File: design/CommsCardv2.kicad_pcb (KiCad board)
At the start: 4 copper layers, 191 parts, among them J1001 USB_B, J201 Conn_01x02, J301 DB9_Male_MountingHoles, J302 DB9_Male_MountingHoles, J303 DB9_Male_MountingHoles, J304 Conn_01x02, J305 Conn_Coaxial, J501 Conn_01x03, J701 Conn_01x03, J901 USB_B, Q301 Q_NMOS_DGS, Q302 Q_NMOS_DGS, U1001 ADUM3160, U201 LT3509EMSE, U301 MAX3387EEUG, U302 MAX3485, U303 TPS28225DRBT, U401 74LV14, U402 74LVC2G00, U403 STWD100xxWY, U404 STWD100xxWY, U405 74AHC157, U501 93C46B, U502 FT4232H, U503 74LV595, U601 74LVC3G14, U602 SN74LV86, U603 501BMILF, U604 74LVC1G80, U605 74LV595, U606 74LV595, U701 93C46B, U702 FT4232H, U703 74LV595, U801 74LVC3G14, U802 SN74LV86, U803 501BMILF, U804 74LVC1G80, U805 74LV595, U806 74LV595, U901 ADUM3160, X501 ASEMB-12MHz, X701 ASEMB-12MHz

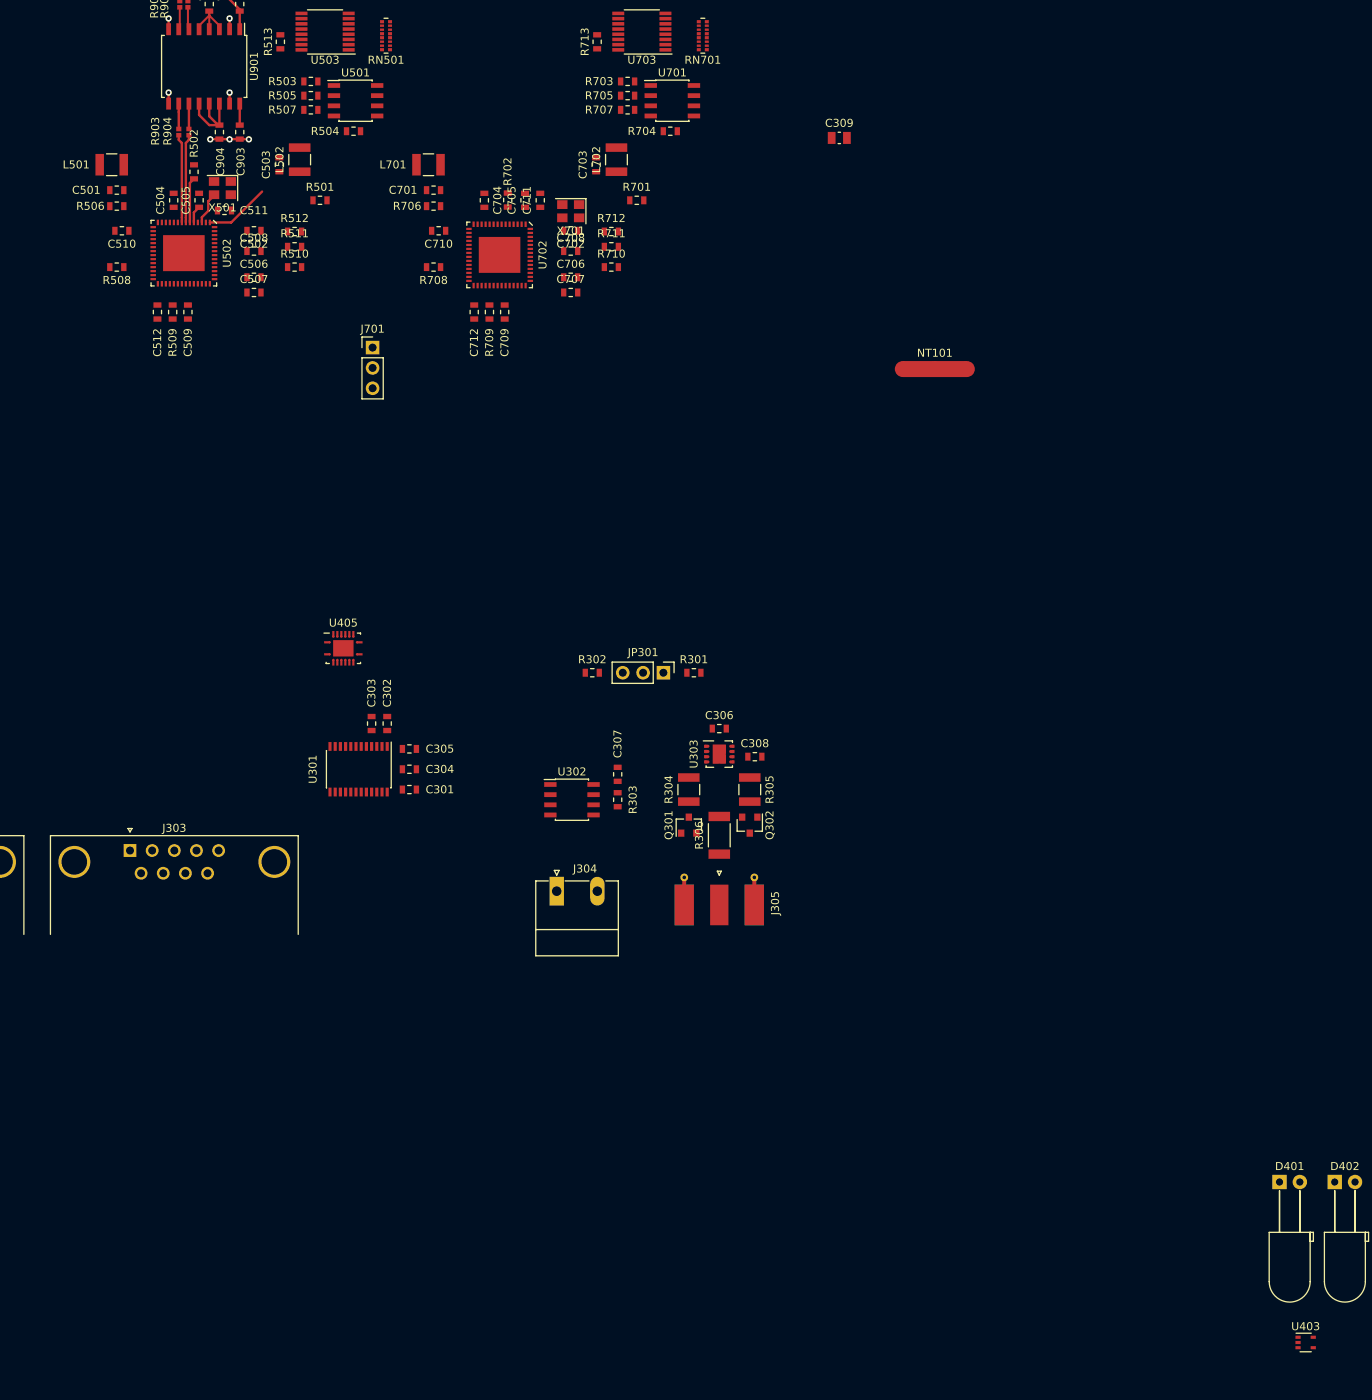
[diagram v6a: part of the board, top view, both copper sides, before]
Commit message: Layout FC1 FT Chip
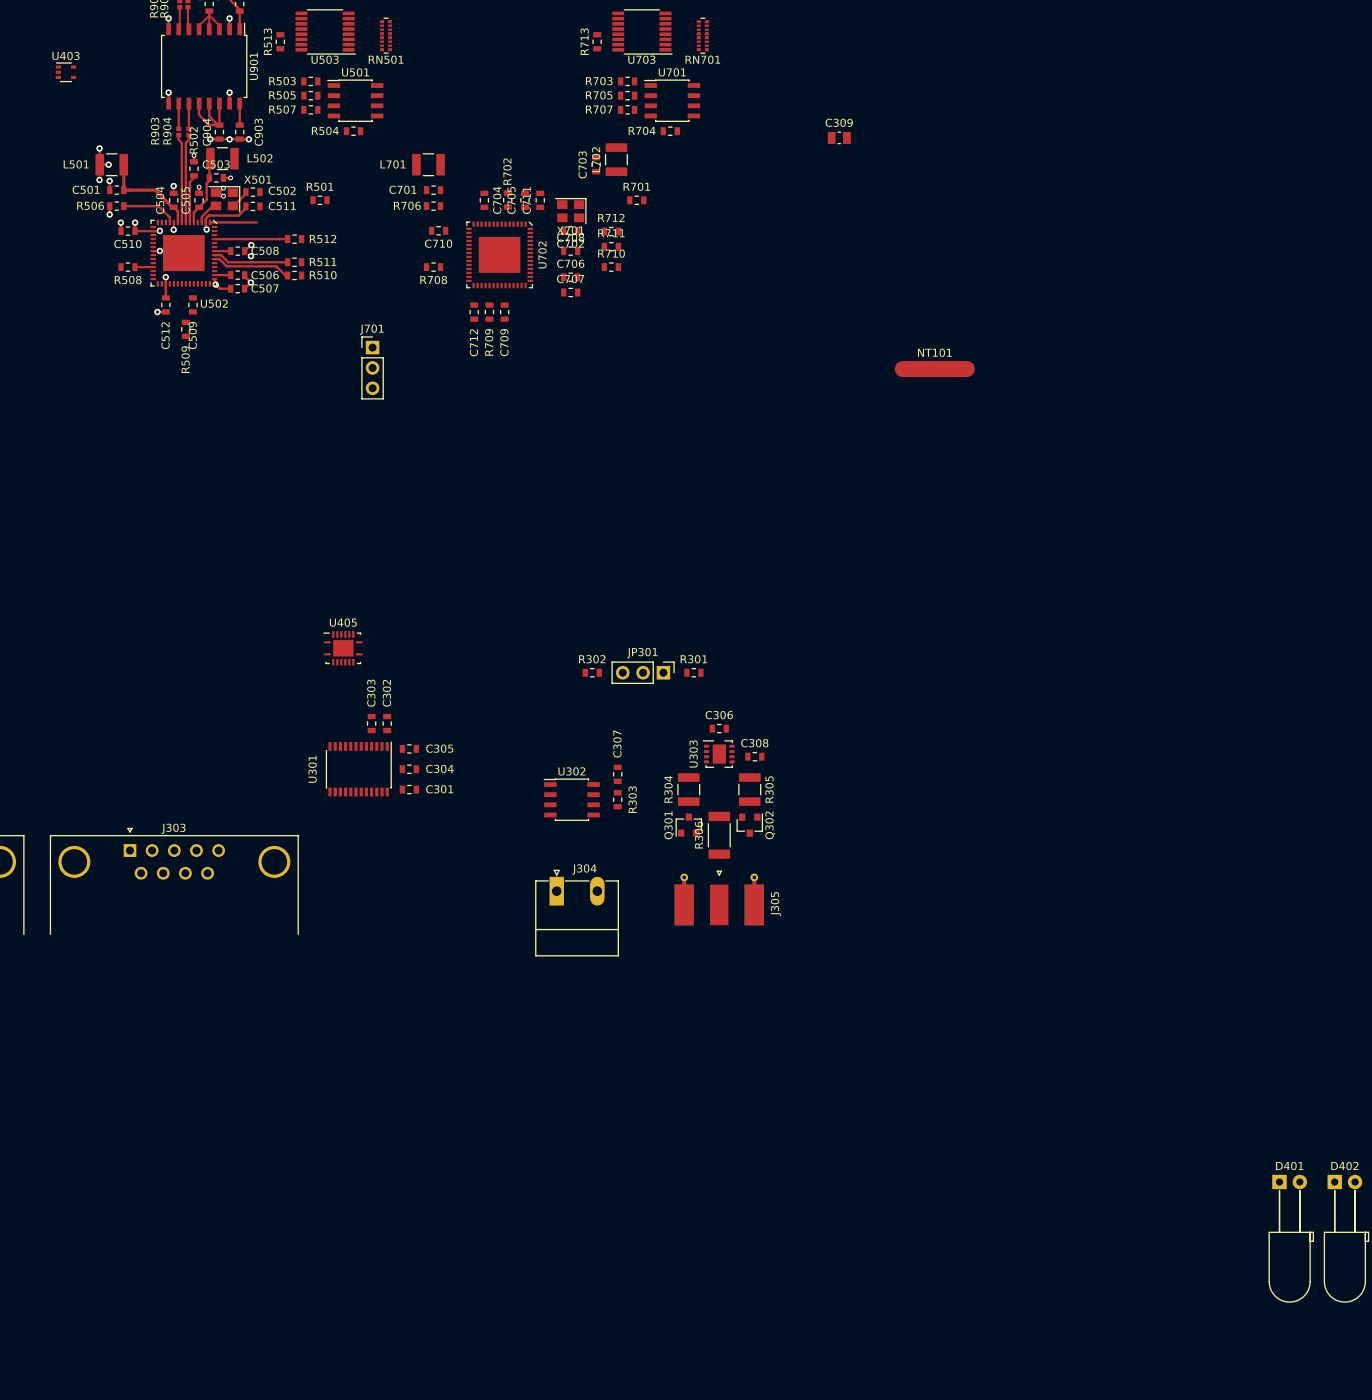
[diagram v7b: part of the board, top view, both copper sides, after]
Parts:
- moved U403 221.9 mm to (150.1, 55.1)
- moved L502 9.65 mm to (169.7, 65.9), turned to 0 degrees
- moved C503 8.05 mm to (168.9, 68.3), turned to 0 degrees
- moved C502 4.83 mm to (173.5, 70.1), turned to 0 degrees
- moved C511 3.59 mm to (173.5, 71.9)
- moved R509 2.72 mm to (165.1, 87.2)
- moved C507 2.09 mm to (171.6, 82.2)
- moved C506 2.05 mm to (171.6, 80.5)
- moved C508 2.03 mm to (171.6, 77.5)
- moved R511 1.94 mm to (178.7, 78.9)
- moved X501 1.42 mm to (169.9, 71.0)
- moved R508 1.40 mm to (157.9, 79.5)
- moved C512 1.38 mm to (162.6, 84.2)
- moved C509 1.09 mm to (166.0, 84.2)
- moved R510 1.05 mm to (178.7, 80.5)
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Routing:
- net +3V3: track 7.26 -> 24.1 mm, vias 2 -> 8
- net GND: track 30.1 -> 44.4 mm, vias 16 -> 30
- net /FlightComputer1/1V8: track 0.00 -> 12.7 mm, vias 0 -> 3
- net Net-(C501-Pad1): track 0.00 -> 12.4 mm
- net Net-(R510-Pad1): track 0.00 -> 9.98 mm
- net Net-(R511-Pad1): track 0.00 -> 9.50 mm
- net Net-(R512-Pad1): track 0.00 -> 9.13 mm
- net Net-(R506-Pad2): track 0.00 -> 6.96 mm
- net Net-(C503-Pad1): track 2.17 -> 8.84 mm
- net Net-(R508-Pad1): track 0.00 -> 2.28 mm
- net /FlightComputer1/EECS: track 8.13 -> 5.87 mm
- net /FlightComputer1/OSCI: track 4.10 -> 3.05 mm
- added copper zone on PWR2.Cu, net +3V3
- added copper zone on PWR2.Cu, net /FlightComputer1/1V8
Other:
- net class GND added: clearance 0.2, trace_width 0.3, via_dia 0.6, via_drill 0.35

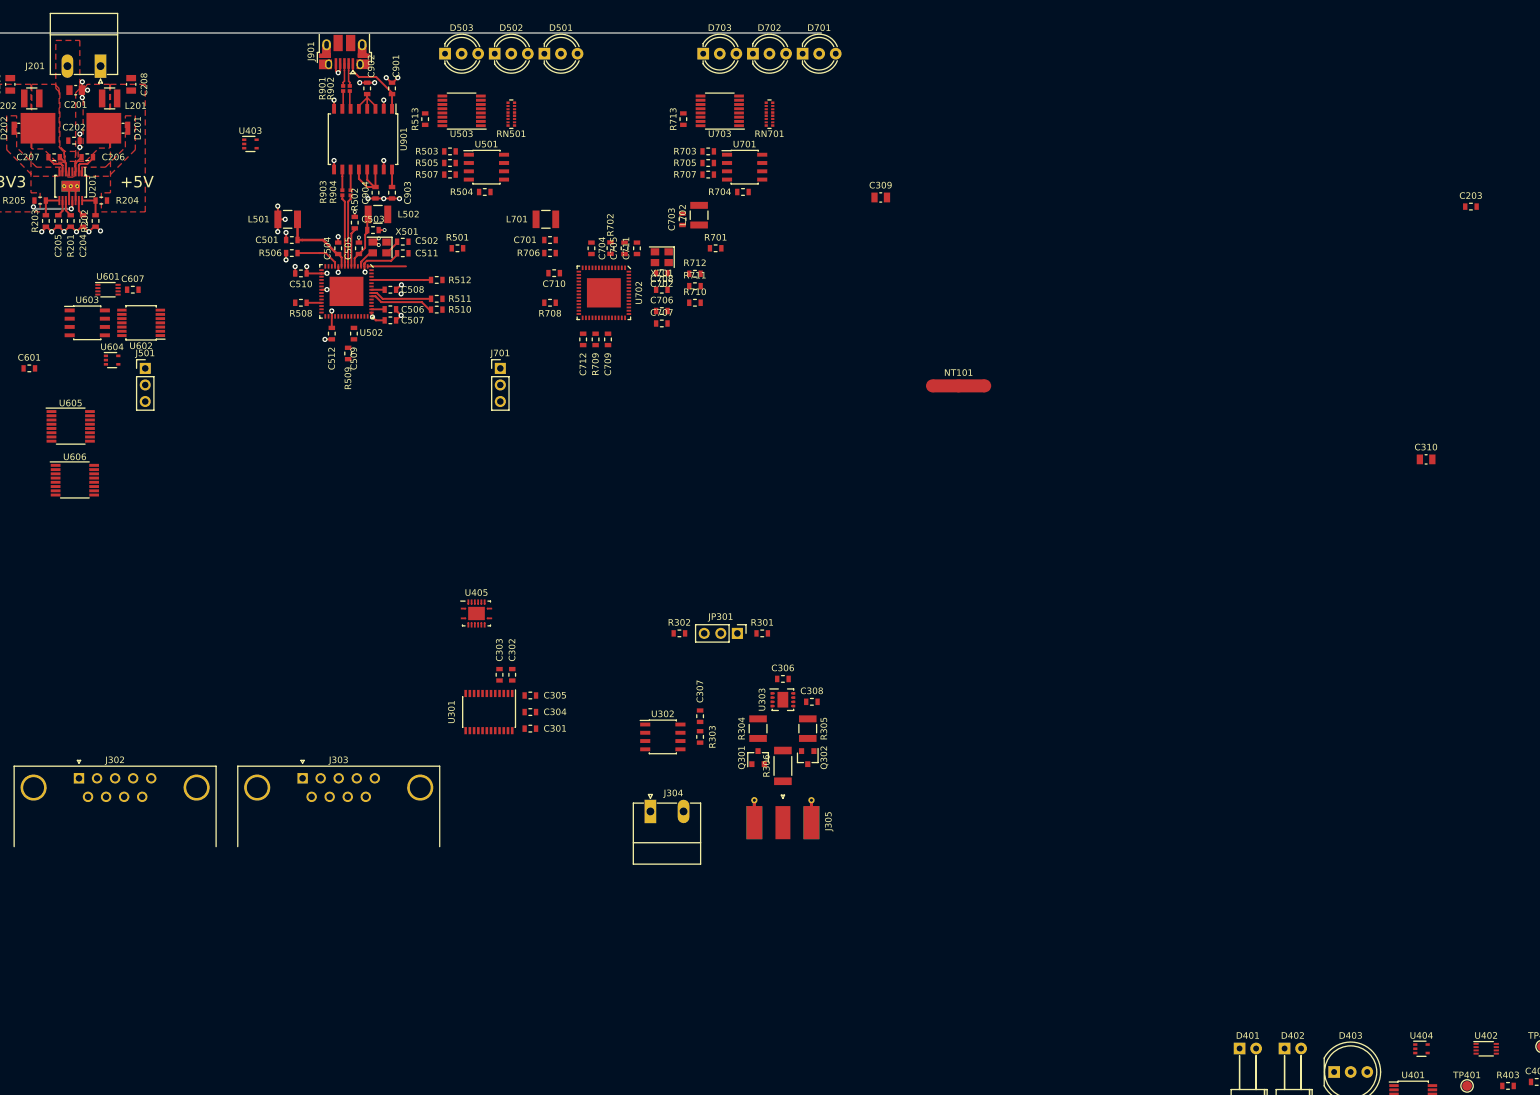
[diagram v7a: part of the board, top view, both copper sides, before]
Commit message: Finish FC1 layout
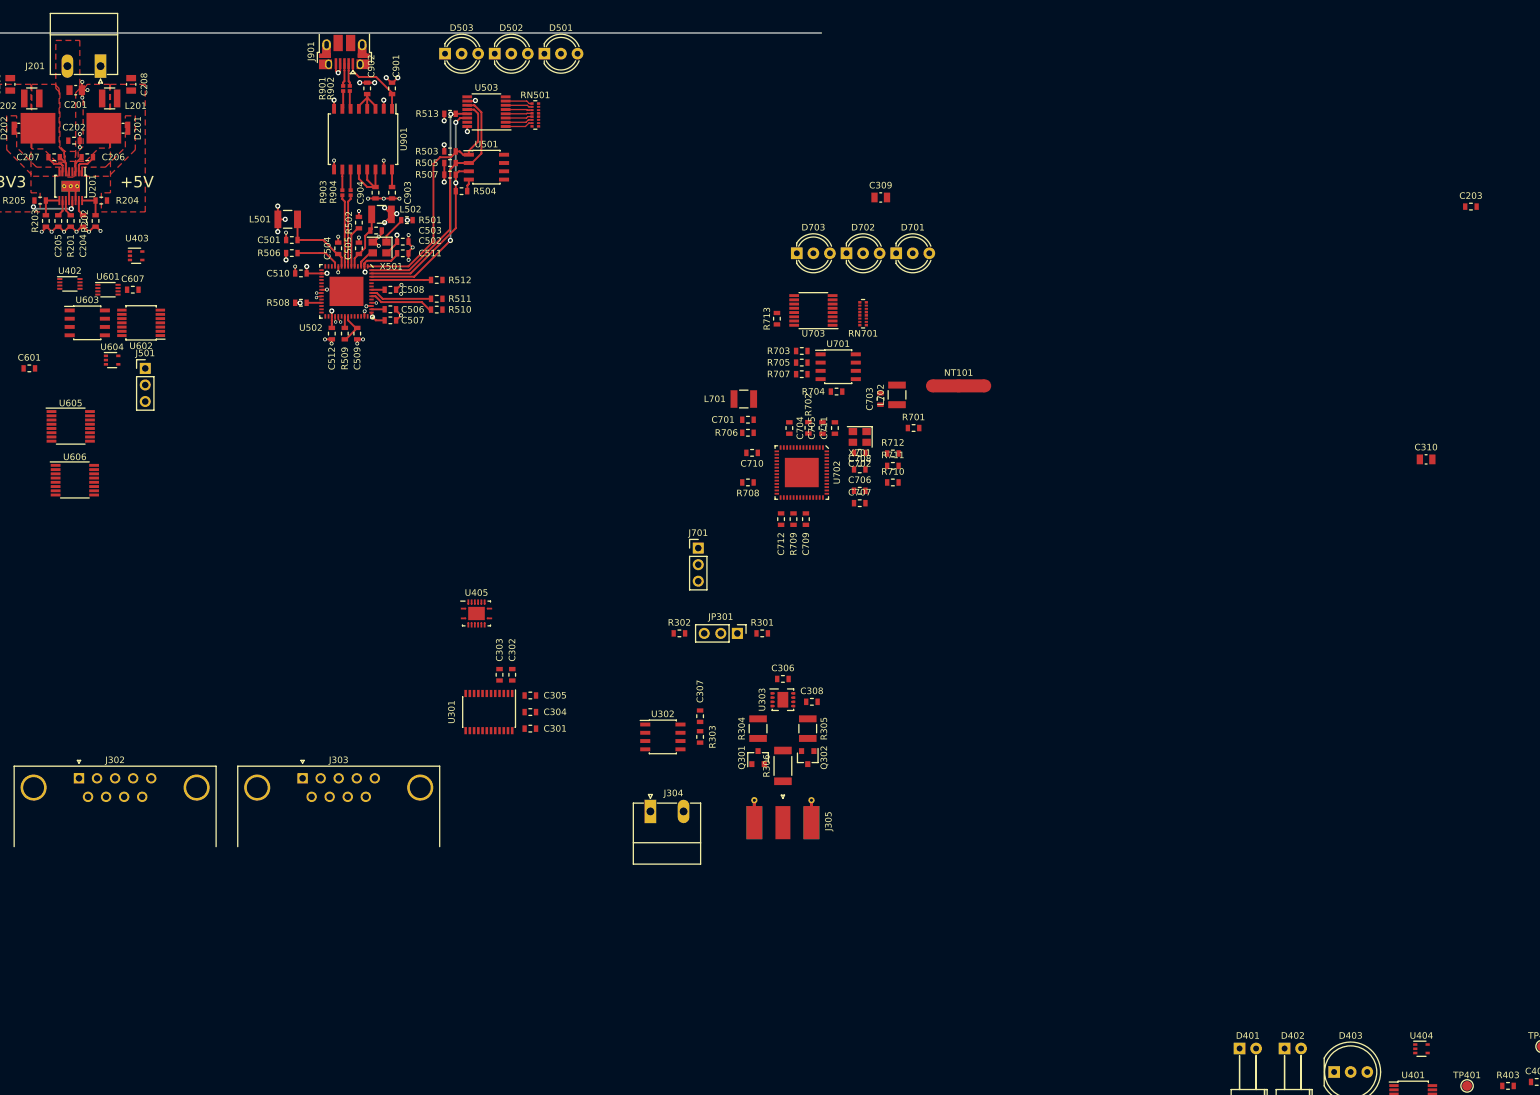
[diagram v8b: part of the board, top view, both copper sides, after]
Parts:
- moved U402 246.8 mm to (122.4, 76.6)
- moved C701 41.0 mm to (226.4, 97.4)
- moved R706 41.0 mm to (226.4, 99.4)
- moved C703 41.0 mm to (246.7, 94.2)
- moved C704 41.0 mm to (232.8, 98.7)
- moved C705 41.0 mm to (237.8, 98.7)
- moved C710 41.0 mm to (227.0, 102.5)
- moved C711 41.0 mm to (239.7, 98.7)
- moved J701 41.0 mm to (218.8, 117.1)
- moved R701 41.0 mm to (251.8, 98.7)
- moved R708 41.0 mm to (226.4, 107.0)
- moved R710 41.0 mm to (248.6, 107.0)
- moved R711 41.0 mm to (248.6, 104.5)
- moved R712 41.0 mm to (248.6, 102.6)
- moved U702 41.0 mm to (234.7, 105.5)
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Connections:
- RN501 pad 10: Net-(D503-Pad1) -> Net-(RN501-Pad10)
- RN501 pad 11: Net-(D502-Pad3) -> Net-(D501-Pad1)
- RN501 pad 12: Net-(D502-Pad1) -> Net-(D501-Pad3)
- RN501 pad 13: Net-(D501-Pad3) -> Net-(D502-Pad1)
- RN501 pad 14: Net-(D501-Pad1) -> Net-(D502-Pad3)
- RN501 pad 15: Net-(RN501-Pad15) -> Net-(D503-Pad1)
- RN501 pad 16: Net-(RN501-Pad16) -> Net-(D503-Pad3)
- RN501 pad 9: Net-(D503-Pad3) -> Net-(RN501-Pad9)
- RN701 pad 10: Net-(D703-Pad1) -> Net-(RN701-Pad10)
- RN701 pad 11: Net-(D702-Pad3) -> Net-(D701-Pad1)
- RN701 pad 12: Net-(D702-Pad1) -> Net-(D701-Pad3)
- RN701 pad 13: Net-(D701-Pad3) -> Net-(D702-Pad1)
- RN701 pad 14: Net-(D701-Pad1) -> Net-(D702-Pad3)
- RN701 pad 15: Net-(RN701-Pad15) -> Net-(D703-Pad1)
- RN701 pad 16: Net-(RN701-Pad16) -> Net-(D703-Pad3)
- RN701 pad 9: Net-(D703-Pad3) -> Net-(RN701-Pad9)
- U503 pad 1: Net-(RN501-Pad2) -> Net-(RN501-Pad7)
- U503 pad 15: Net-(RN501-Pad1) -> Net-(RN501-Pad8)
- U503 pad 2: Net-(RN501-Pad3) -> Net-(RN501-Pad6)
- U503 pad 3: Net-(RN501-Pad4) -> Net-(RN501-Pad5)
- U503 pad 4: Net-(RN501-Pad5) -> Net-(RN501-Pad4)
- U503 pad 5: Net-(RN501-Pad6) -> Net-(RN501-Pad3)
- U503 pad 6: Net-(RN501-Pad7) -> Net-(RN501-Pad2)
- U503 pad 7: Net-(RN501-Pad8) -> Net-(RN501-Pad1)
- U703 pad 1: Net-(RN701-Pad2) -> Net-(RN701-Pad7)
- U703 pad 15: Net-(RN701-Pad1) -> Net-(RN701-Pad8)
- U703 pad 2: Net-(RN701-Pad3) -> Net-(RN701-Pad6)
- U703 pad 3: Net-(RN701-Pad4) -> Net-(RN701-Pad5)
- U703 pad 4: Net-(RN701-Pad5) -> Net-(RN701-Pad4)
- U703 pad 5: Net-(RN701-Pad6) -> Net-(RN701-Pad3)
- U703 pad 6: Net-(RN701-Pad7) -> Net-(RN701-Pad2)
- U703 pad 7: Net-(RN701-Pad8) -> Net-(RN701-Pad1)
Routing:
- net /FlightComputer1/EECLK: track 0.00 -> 38.7 mm
- net /FlightComputer1/EEDATA: track 0.00 -> 38.0 mm, vias 0 -> 2
- net /Watchdog/~FC1_PWREN: track 0.00 -> 36.3 mm, vias 0 -> 2
- net /FlightComputer1/EECS: track 5.87 -> 38.9 mm
- net +3V3: track 24.1 -> 42.9 mm, vias 8 -> 19
- net GND: track 44.4 -> 53.8 mm, vias 30 -> 37
- net Net-(R501-Pad1): track 0.00 -> 4.30 mm
- net Net-(RN501-Pad7): track 0.00 -> 4.26 mm
- net Net-(RN501-Pad1): track 0.00 -> 4.20 mm
- net Net-(RN501-Pad6): track 0.00 -> 4.20 mm
- net Net-(RN501-Pad2): track 0.00 -> 4.14 mm
- net Net-(RN501-Pad5): track 0.00 -> 4.13 mm
- net Net-(RN501-Pad3): track 0.00 -> 4.08 mm
- net Net-(RN501-Pad4): track 0.00 -> 4.07 mm
- net Net-(R504-Pad1): track 0.00 -> 2.02 mm
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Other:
- net class ThinNet: via_dia 0.6 -> 0.5; via_drill 0.35 -> 0.3
